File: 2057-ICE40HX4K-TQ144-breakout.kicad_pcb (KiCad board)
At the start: 4 copper layers, 99.1 x 66 mm, 75 parts, among them J1 Conn_02x30_Odd_Even, J2 Conn_02x30_Odd_Even, J3 RaspberryPI-B+header, J4 USB4105-GF-A, J5 RaspberryPI-B+header, J6 Conn_02x08_Odd_Even, J7 Conn_02x01, J8 Micro_SD_Card_Det, U1 ICE40HX4K-TQ144, U2 AZ1117CH-3.3TRG1, U3 AZ1117CH-1.2, U4 AT45DB161D-SU, Y1 XLH536025_000000I

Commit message: Update to KiCad version 10 format
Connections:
- net /~CRESET~ renamed /~{CRESET}
- net /~FRESET~ renamed /~{FRESET}
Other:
- net class Default removed
- board text added: "~{CRESET}"
- board text added: "~{FRESET}"
- board text removed: "~CRESET"
- board text removed: "~FRESET"

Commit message: Fix power vias
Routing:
- net +3V3: track 103.8 -> 107.9 mm
- net +1V2: track 123.6 -> 125.4 mm

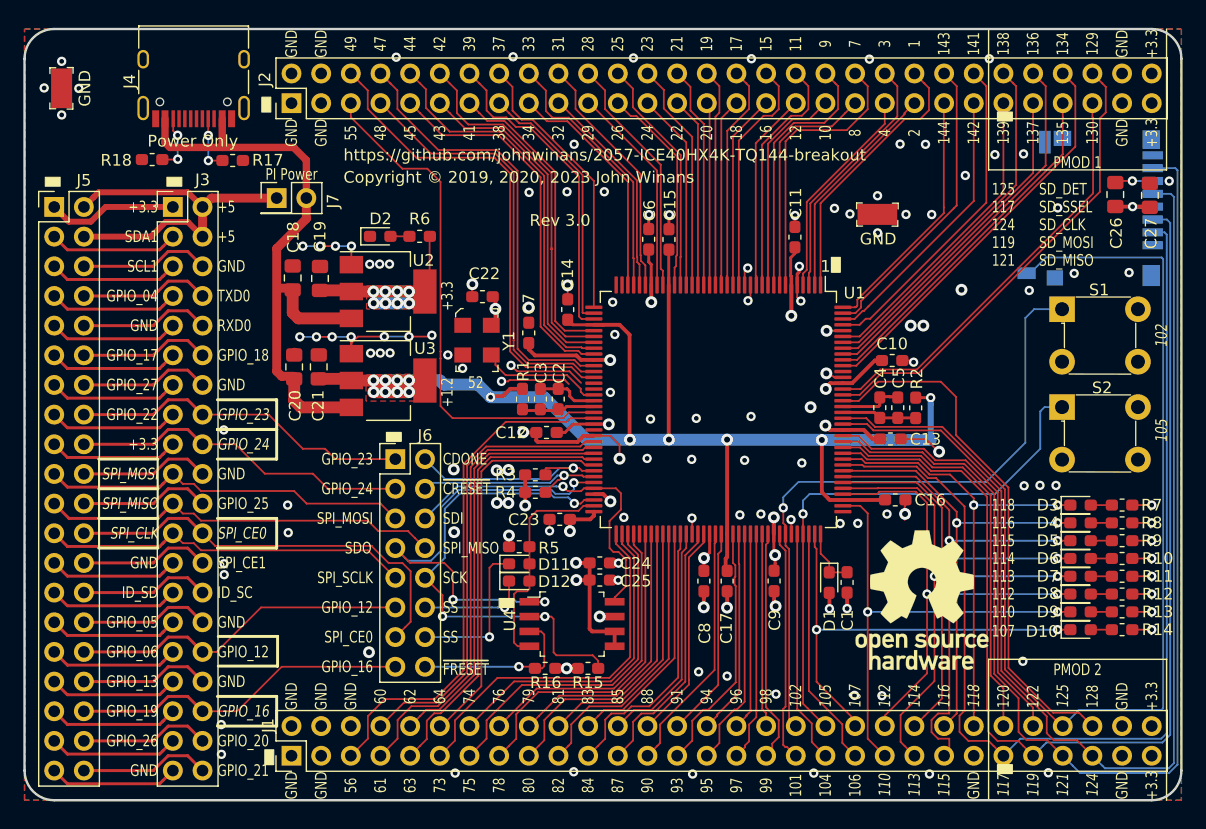
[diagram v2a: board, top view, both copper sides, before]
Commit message: Fix co-linear tracks
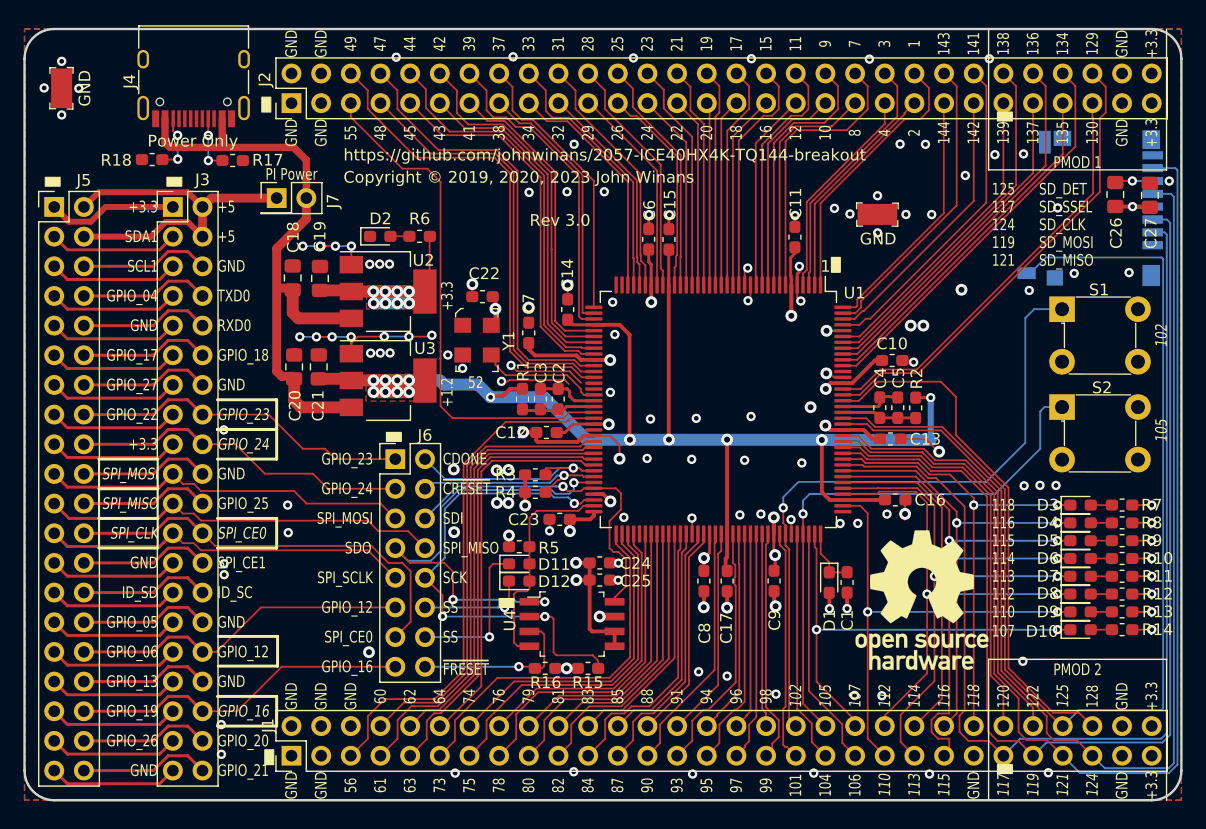
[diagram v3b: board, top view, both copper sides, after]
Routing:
- net /IOT_173: track 40.5 -> 39.7 mm
- net /IOL_12B: track 16.9 -> 16.1 mm
- net /IOT_170: track 44.0 -> 43.2 mm

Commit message: Updated gerbers+drill files
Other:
- rule pad_to_mask_clearance: 0.0254 -> 0
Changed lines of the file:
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@@
 	)
 	(setup
-		(pad_to_mask_clearance 0.0254)
-		(solder_mask_min_width 0.1016)
+		(pad_to_mask_clearance 0)
 		(allow_soldermask_bridges_in_footprints no)
 		(tenting
